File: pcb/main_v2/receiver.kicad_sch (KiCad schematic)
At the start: 14 parts, among them IC401 RMS-30+, IC402 HMC374, J401 Conn_Coaxial, J402 Conn_Coaxial

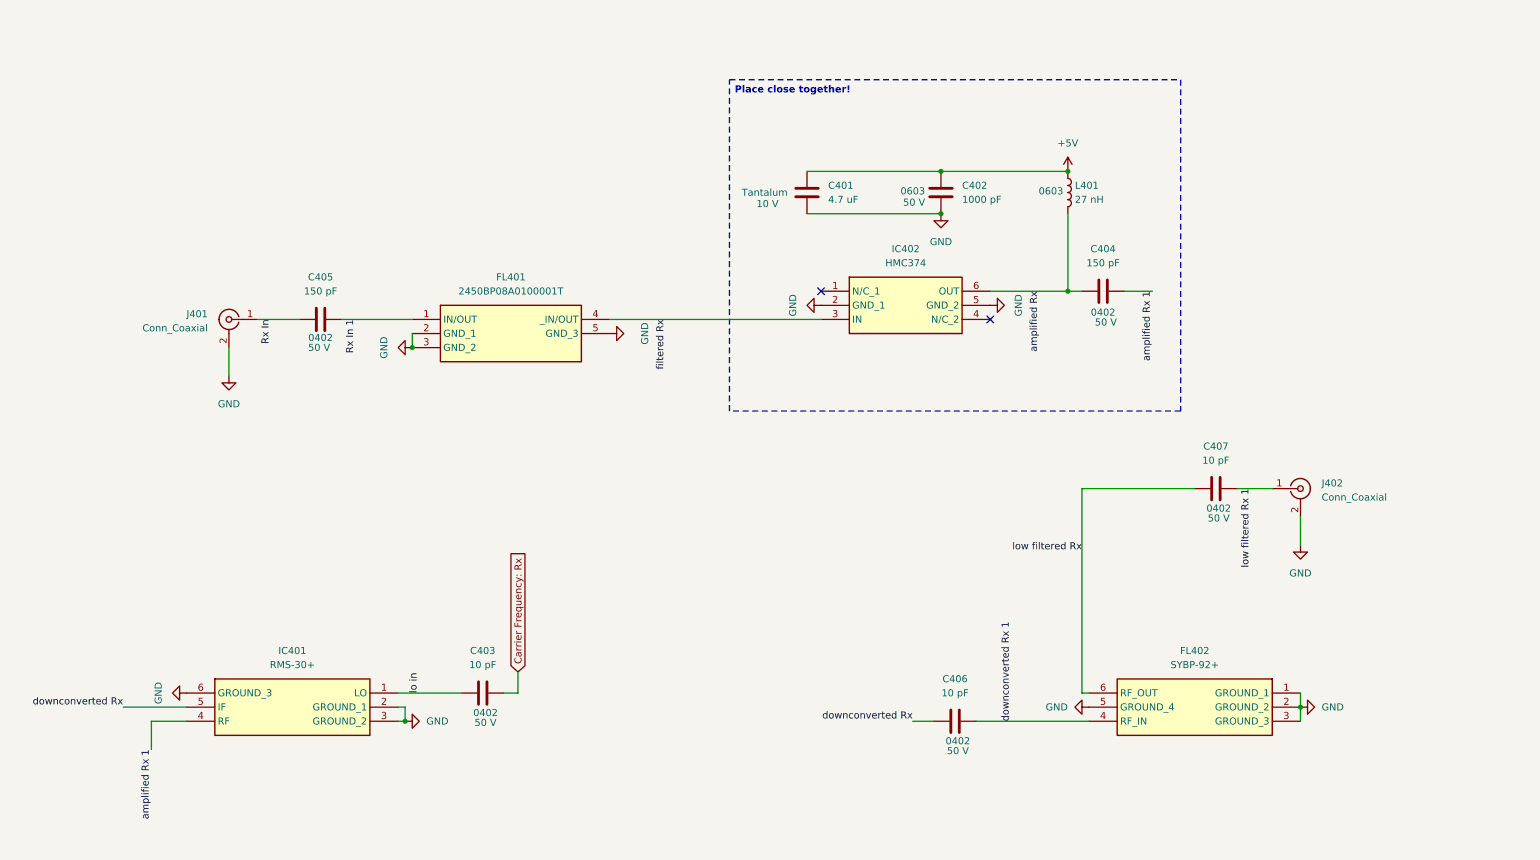
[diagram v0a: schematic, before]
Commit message: updated layout
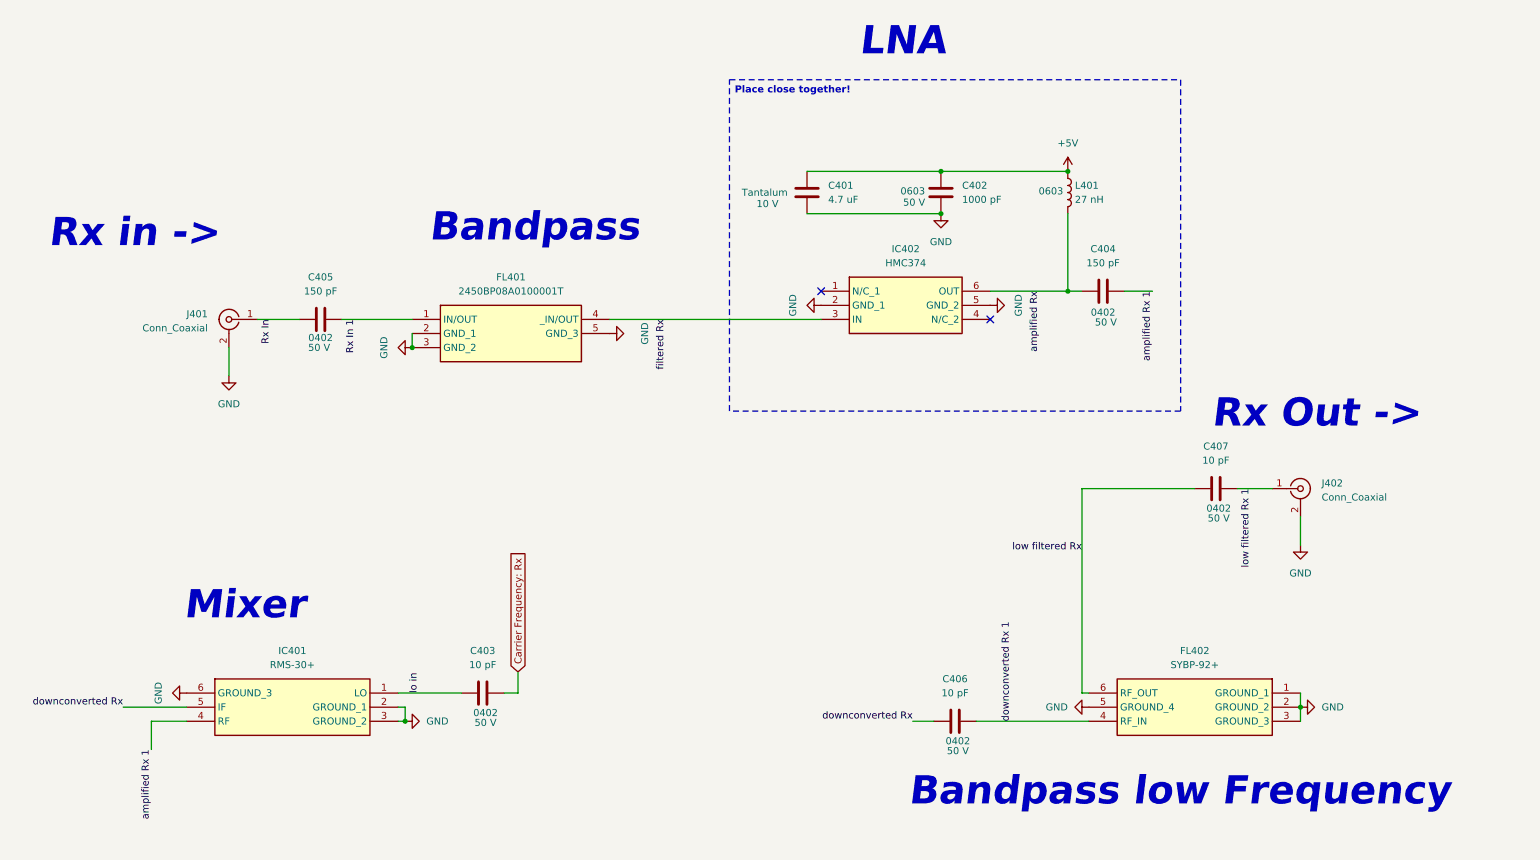
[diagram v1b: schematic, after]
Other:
- note added: "Bandpass"
- note added: "Bandpass low Frequency"
- note added: "LNA"
- note added: "Mixer"
- note added: "Rx Out ->"
- note added: "Rx in ->"
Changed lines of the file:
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@@
 	(generator_version "10.0")
 	(paper "A4")
+	(text "Bandpass low Frequency"
+		(exclude_from_sim no)
+		(at 185.928 158.75 0)
+		(effects
+			(font
+				(size 5.08 5.08)
+				(thickness 0.254)
+				(bold yes)
+				(italic yes)
+				(color 62 180 4 1)
+			)
+			(justify left)
+		)
+	)
+	(text "Rx in ->"
+		(exclude_from_sim no)
+		(at 30.988 58.166 0)
+		(effects
+			(font
+				(size 5.08 5.08)
+				(thickness 0.254)
+				(bold yes)
+				(italic yes)
+				(color 62 180 4 1)
+			)
+			(justify left)
+		)
+	)
+	(text "LNA"
+		(exclude_from_sim no)
+		(at 177.038 23.622 0)
+		(effects
+			(font
+				(size 5.08 5.08)
+				(thickness 0.254)
+				(bold yes)
+				(italic yes)
+				(color 62 180 4 1)
+			)
+			(justify left)
+		)
+	)
+	(text "Bandpass"
+		(exclude_from_sim no)
+		(at 99.568 57.15 0)
+		(effects
+			(font
+				(size 5.08 5.08)
+				(thickness 0.254)
+				(bold yes)
+				(italic yes)
+				(color 62 180 4 1)
+			)
+			(justify left)
+		)
+	)
+	(text "Rx Out ->"
+		(exclude_from_sim no)
+		(at 240.538 90.678 0)
+		(effects
+			(font
+				(size 5.08 5.08)
+				(thickness 0.254)
+				(bold yes)
+				(italic yes)
+				(color 62 180 4 1)
+			)
+			(justify left)
+		)
+	)
+	(text "Mixer"
+		(exclude_from_sim no)
+		(at 55.372 125.222 0)
+		(effects
+			(font
+				(size 5.08 5.08)
+				(thickness 0.254)
+				(bold yes)
+				(italic yes)
+				(color 62 180 4 1)
+			)
+			(justify left)
+		)
+	)
 	(text_box "Place close together!"
 		(exclude_from_sim no)
